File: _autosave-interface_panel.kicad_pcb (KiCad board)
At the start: 2 copper layers, 50.6 x 29.8 mm, 13 parts, among them J1 Conn_02x04_Odd_Even

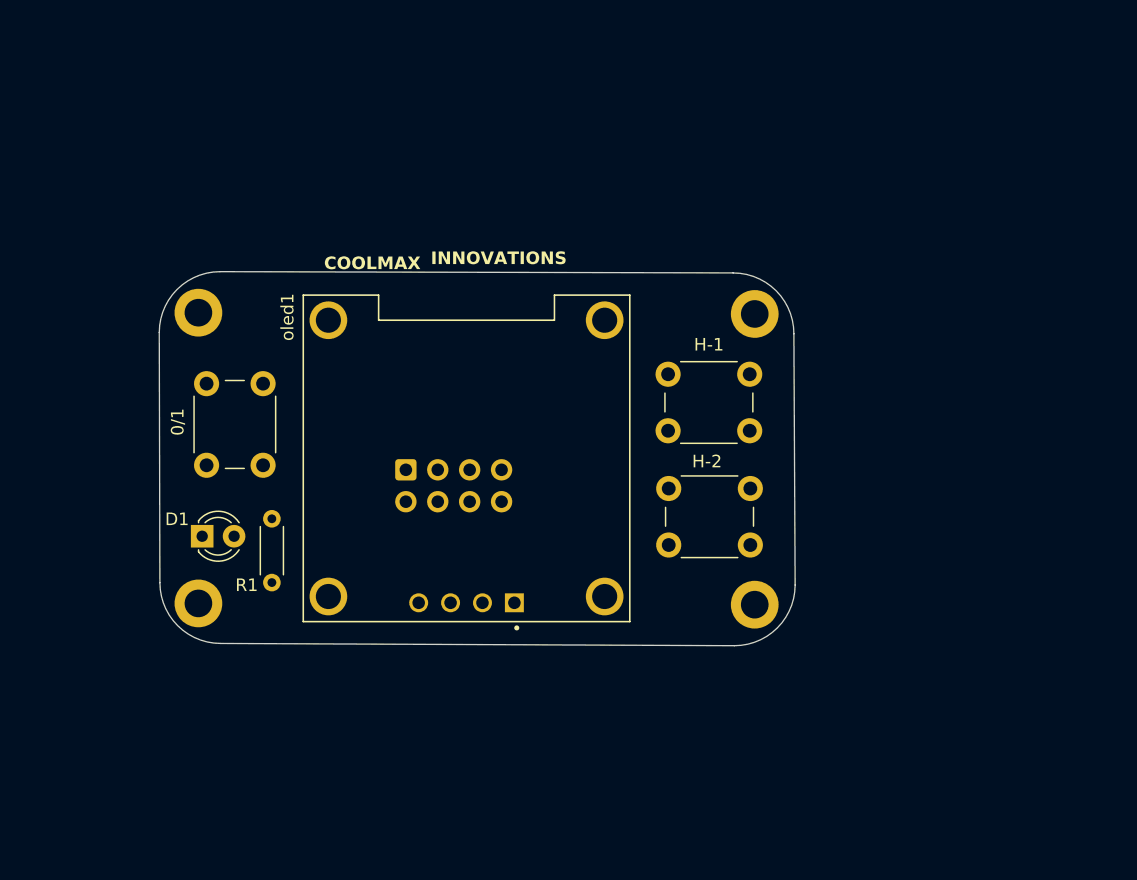
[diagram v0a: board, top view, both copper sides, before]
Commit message: display and overall layout changed
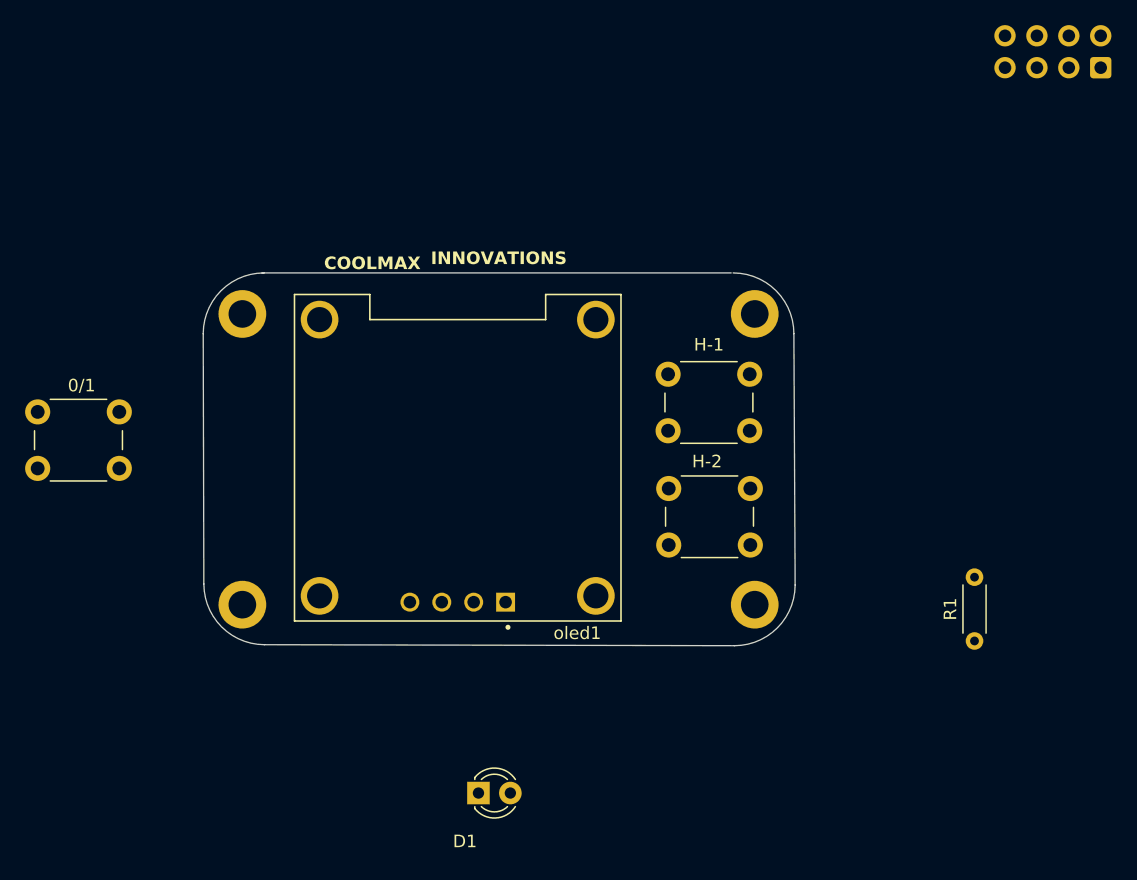
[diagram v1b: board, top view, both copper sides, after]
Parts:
- moved J1 63.9 mm to (193.6, 44.0), turned to 90 degrees
- moved R1 56.1 mm to (183.5, 89.7)
- moved D1 30.0 mm to (144.0, 101.8)
- moved 0/1 13.3 mm to (115.4, 76.0), turned to 180 degrees
- moved REF** 3.50 mm to (125.2, 63.6)
- moved REF** 3.50 mm to (125.2, 86.8)
- moved oled1 0.70 mm to (142.3, 75.1)
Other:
- board size 50.6 x 29.8 mm -> 47.1 x 29.7 mm
